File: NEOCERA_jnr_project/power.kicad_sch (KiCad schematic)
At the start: 26 parts, among them J1 USB_B, J3 770967-2, J4 770967-2, U10 LM7805_TO220, U11 LD39150DT33, U8 FT231XS, U9 HCPL-2630

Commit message: Update power.kicad_sch
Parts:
- added C17: 470uf, Capacitor_SMD:C_0603_1608Metric_Pad1.08x0.95mm_HandSolder, symbol Device:C_Polarized_US
- added C18, C20, C23, C25: 0.1uf, Capacitor_SMD:C_0603_1608Metric_Pad1.08x0.95mm_HandSolder, symbol Device:C_Polarized_US
- added C19, C21, C22, C24, C26: 10uf, Capacitor_SMD:C_0603_1608Metric_Pad1.08x0.95mm_HandSolder, symbol Device:C
- added C27: 22uf, Capacitor_SMD:C_0603_1608Metric_Pad1.08x0.95mm_HandSolder, symbol Device:C
- added C28, C29, C30, C31: 0.1uf, Capacitor_SMD:C_0603_1608Metric_Pad1.08x0.95mm_HandSolder, symbol Device:C
- added CR1: DLP05LC-7-F, SOT23_DLP05LC_DIO, symbol DLP05LC:DLP05LC-7-F
- added D3: D_Schottky_Filled, Diode_SMD:D_2114_3652Metric, symbol Device:D_Schottky_Filled
- added FB3: FerriteBead, Ferrite_THT:LairdTech_28C0236-0JW-10, symbol Device:FerriteBead
- added R25, R26, R27, R28: 27, Resistor_SMD:R_1206_3216Metric, symbol Device:R_Small_US
- added R29: 1500, Resistor_SMD:R_1206_3216Metric, symbol Device:R_Small_US
- added TP1, TP13, TP14: TestPoint, TestPoint:TestPoint_Loop_D2.50mm_Drill1.0mm, symbol Connector:TestPoint
- added U12: HCPL-2630, Package_DIP:DIP-8_W7.62mm, symbol Isolator:HCPL-2630
- C11, C12, C13, C14, C15, C16: footprint (none) -> Capacitor_SMD:C_0603_1608Metric_Pad1.08x0.95mm_HandSolder
- FB1, FB2: footprint (none) -> Ferrite_THT:LairdTech_28C0236-0JW-10
- J1: footprint (none) -> Connector_USB:USB_B_OST_USB-B1HSxx_Horizontal
- R14, R15, R16, R18, R20, R21, R22, R23, R24: footprint (none) -> Resistor_SMD:R_1206_3216Metric
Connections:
- net Earth: now also J3.2, J4.2, U10.2 (GND), C17.2, C18.2, C19.2, C20.2, C21.2, C22.2, C23.2, C24.2, C25.2, C26.2, C27.2, CR1.1 (G), R28.1
- net USB: now also C28.2, C29.2, C30.2, C31.2, U12.5 (GND)
- net at J4.1: now also J3.1, R25.2
- net at J4.3: now also FB2.1, J3.3
- net at U11.1 (VI): now also U10.3 (VO), C25.1, C26.1, C27.1, CR1.3, D3.1 (K), TP1.1
- net at U11.3 (VO): now also C22.1, C23.1, C24.1, D3.2 (A), TP13.1
- net at FB2.2: now also C17.1, C18.1, C19.1, FB3.1
- net at U10.1 (VI): now also C20.1, C21.1, FB3.2, TP14.1
- net at U8.4 (RXD): now also R29.1, U12.7 (VO1)
- new net: C28.1, C29.1, C30.1
- new net: C31.1, U12.8 (VCC)
- new net: R27.1, R28.2
- new net: R26.1, R27.2
- new net: R25.1, R26.2
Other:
- moved on the sheet: C14, C15, FB2, J3, J4, U10, U11

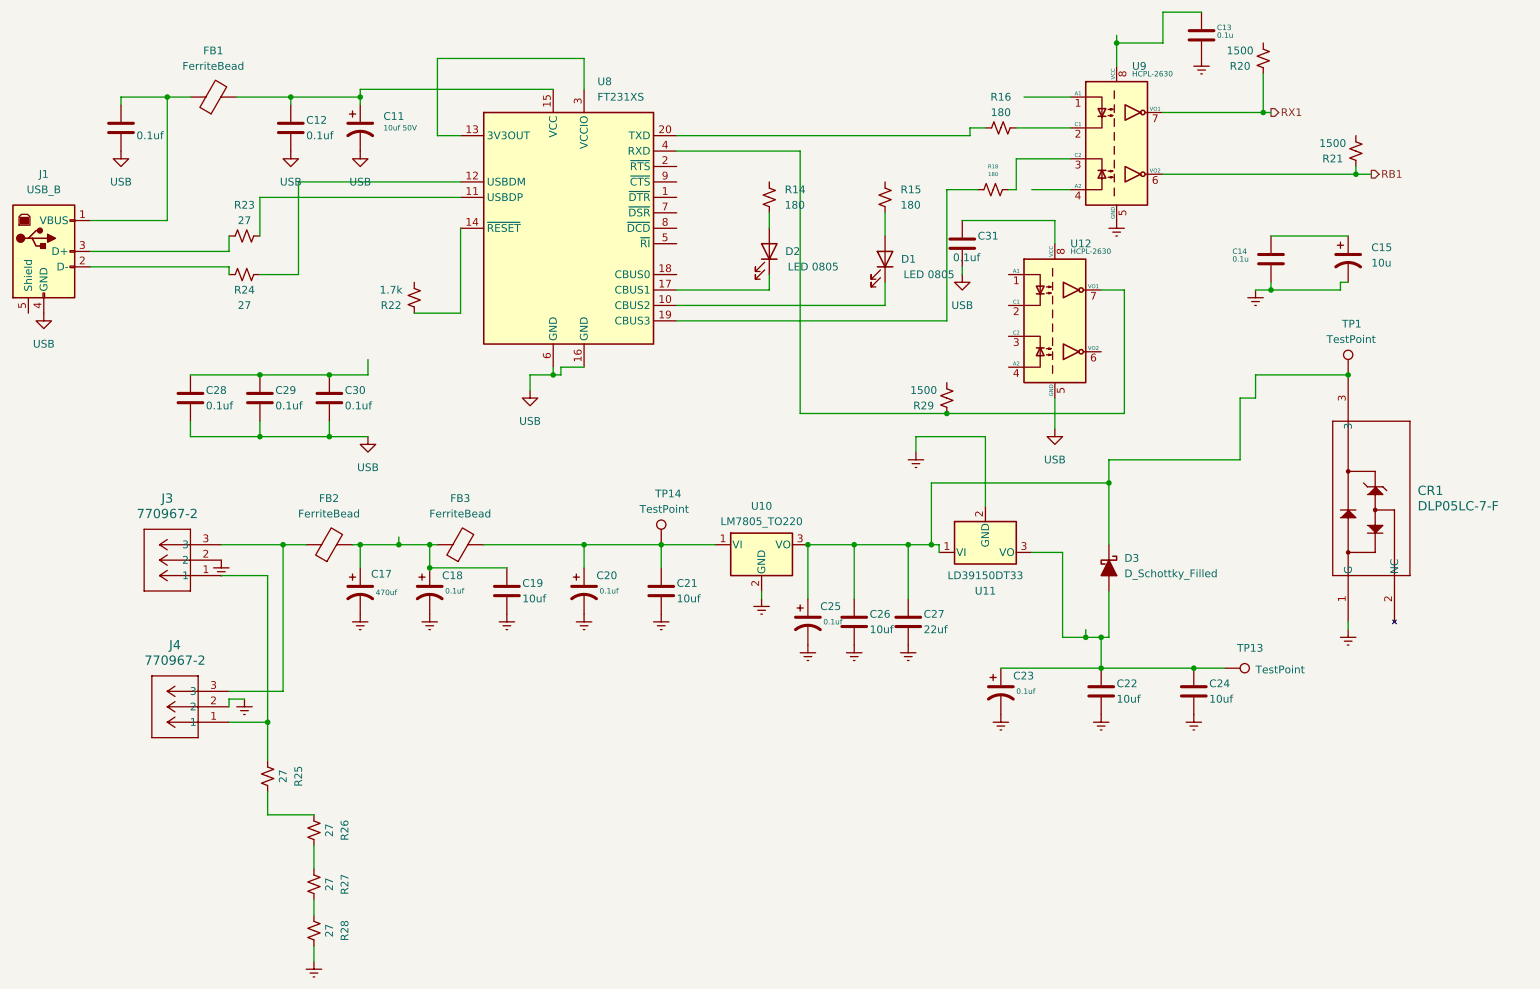
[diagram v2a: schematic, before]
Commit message: changes
edited symbols and usb schematic
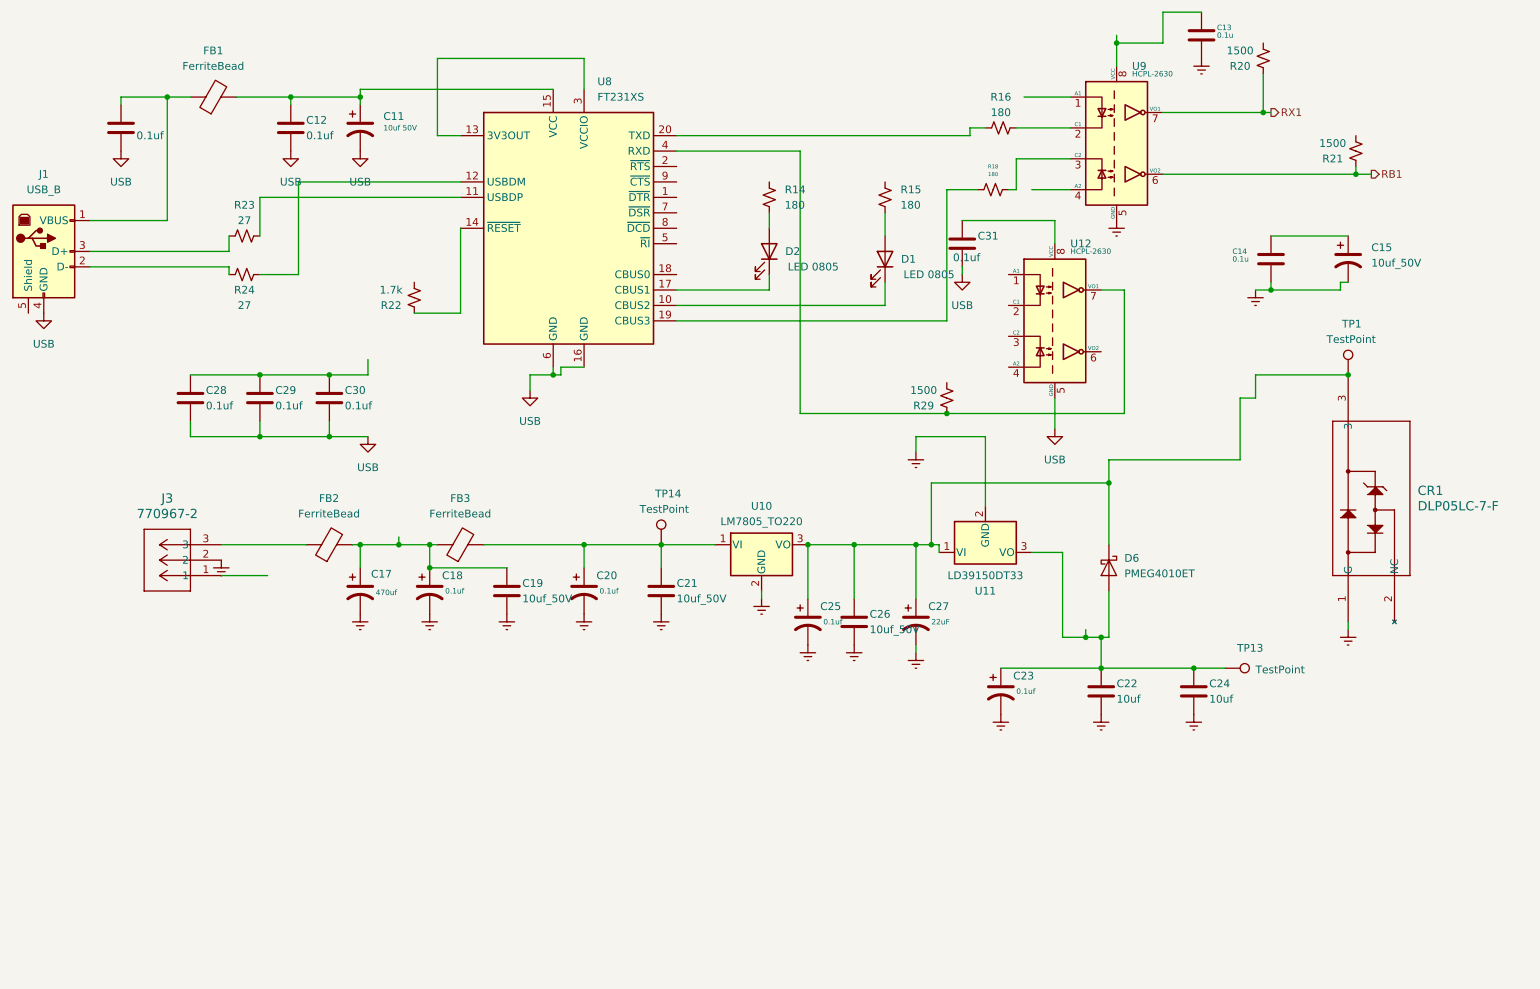
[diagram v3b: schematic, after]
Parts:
- removed C27: 22uf, Capacitor_SMD:C_0603_1608Metric_Pad1.08x0.95mm_HandSolder, symbol Device:C
- removed D3: D_Schottky_Filled, Diode_SMD:D_2114_3652Metric, symbol Device:D_Schottky_Filled
- removed J4: 770967-2, footprints:CONN3_770967-2_TEC, symbol 770967-2:770967-2
- removed R25, R26, R27, R28: 27, Resistor_SMD:R_1206_3216Metric, symbol Device:R_Small_US
- added C27: 22uF, Capacitor_SMD:C_Elec_6.3x5.8, symbol Device:C_Polarized_US
- added D6: PMEG4010ET, Package_TO_SOT_SMD:SOT-23, symbol Diode:PMEG4010ET
- C15: value 10u -> 10uf_50V; footprint Capacitor_SMD:C_0603_1608Metric_Pad1.08x0.95mm_HandSolder -> Capacitor_SMD:C_1206_3216Metric_Pad1.33x1.80mm_HandSolder
- C17: footprint Capacitor_SMD:C_0603_1608Metric_Pad1.08x0.95mm_HandSolder -> (none)
- C19, C21, C26: value 10uf -> 10uf_50V; footprint Capacitor_SMD:C_0603_1608Metric_Pad1.08x0.95mm_HandSolder -> Capacitor_SMD:C_1206_3216Metric_Pad1.33x1.80mm_HandSolder
- D1, D2: footprint LED_SMD:LED_1206_3216Metric_Pad1.42x1.75mm_HandSolder -> LED_SMD:LED_0805_2012Metric_Pad1.15x1.40mm_HandSolder
- R14, R15, R16, R18, R20, R21, R22, R23, R24, R29: footprint Resistor_SMD:R_1206_3216Metric -> Resistor_SMD:R_0603_1608Metric_Pad0.98x0.95mm_HandSolder
- TP1, TP13, TP14: footprint TestPoint:TestPoint_Loop_D2.50mm_Drill1.0mm -> TestPoint:TestPoint_THTPad_D3.0mm_Drill1.5mm
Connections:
- net Earth: now also C27.2
- net at C25.1, C26.1, CR1.3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: now also C27.1, D6.3 (K)
- net at C22.1, C23.1, C24.1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: now also D6.1 (A)

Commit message: symbols changed
edited all symbols
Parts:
- C15, C19, C21, C26: footprint Capacitor_SMD:C_1206_3216Metric_Pad1.33x1.80mm_HandSolder -> Capacitor_SMD:C_0603_1608Metric_Pad1.08x0.95mm_HandSolder
- C17: footprint (none) -> Capacitor_SMD:C_0603_1608Metric_Pad1.08x0.95mm_HandSolder
- C27: footprint Capacitor_SMD:C_Elec_6.3x5.8 -> Capacitor_SMD:C_0603_1608Metric_Pad1.08x0.95mm_HandSolder
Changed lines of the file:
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@@
 			)
 		)
-		(property "Footprint" ""
+		(property "Footprint" "Capacitor_SMD:C_0603_1608Metric_Pad1.08x0.95mm_HandSolder"
 			(at 85.09 110.49 0)
 			(effects
@@
 			)
 		)
-		(property "Footprint" "Capacitor_SMD:C_1206_3216Metric_Pad1.33x1.80mm_HandSolder"
+		(property "Footprint" "Capacitor_SMD:C_0603_1608Metric_Pad1.08x0.95mm_HandSolder"
 			(at 110.1852 114.3 0)
 			(effects
@@
 			)
 		)
-		(property "Footprint" "Capacitor_SMD:C_Elec_6.3x5.8"
+		(property "Footprint" "Capacitor_SMD:C_0603_1608Metric_Pad1.08x0.95mm_HandSolder"
 			(at 176.53 115.57 0)
 			(effects
@@
 			)
 		)
-		(property "Footprint" "Capacitor_SMD:C_1206_3216Metric_Pad1.33x1.80mm_HandSolder"
+		(property "Footprint" "Capacitor_SMD:C_0603_1608Metric_Pad1.08x0.95mm_HandSolder"
 			(at 167.3352 119.38 0)
 			(effects
@@
 			)
 		)
-		(property "Footprint" "Capacitor_SMD:C_1206_3216Metric_Pad1.33x1.80mm_HandSolder"
+		(property "Footprint" "Capacitor_SMD:C_0603_1608Metric_Pad1.08x0.95mm_HandSolder"
 			(at 135.5852 114.3 0)
 			(effects
@@
 			)
 		)
-		(property "Footprint" "Capacitor_SMD:C_1206_3216Metric_Pad1.33x1.80mm_HandSolder"
+		(property "Footprint" "Capacitor_SMD:C_0603_1608Metric_Pad1.08x0.95mm_HandSolder"
 			(at 247.65 55.88 0)
 			(effects
